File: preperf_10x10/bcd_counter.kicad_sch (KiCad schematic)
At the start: 9 parts, among them U8 4511, U9 D168K

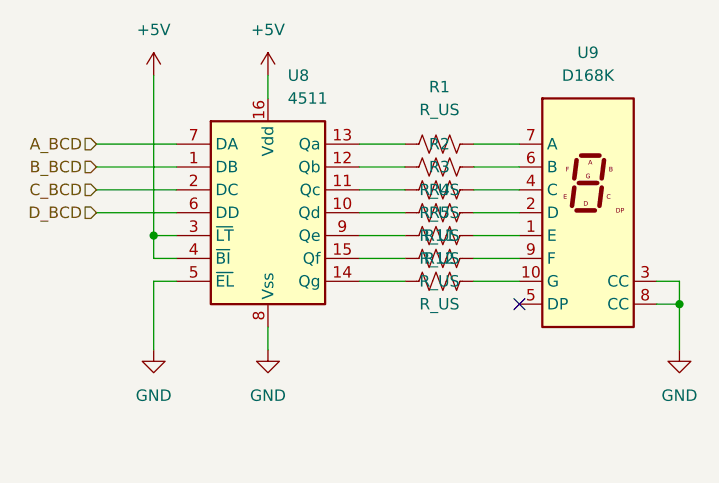
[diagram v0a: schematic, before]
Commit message: "TP2" and "TP3" digital techniques
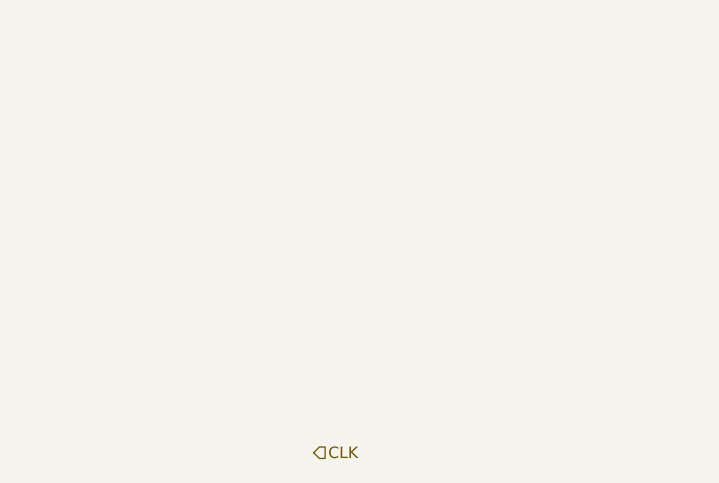
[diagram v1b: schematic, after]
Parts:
- removed R1, R11, R12, R2, R3, R4, R5: R_US, Resistor_THT:R_Axial_DIN0207_L6.3mm_D2.5mm_P2.54mm_Vertical, symbol Device:R_US
- removed U8: 4511, Package_DIP:DIP-16_W7.62mm_Socket, symbol 4xxx_IEEE:4511
- removed U9: D168K, Display_7Segment:D1X8K, symbol Display_Character:D168K
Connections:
- no-connect marks 1 -> 0

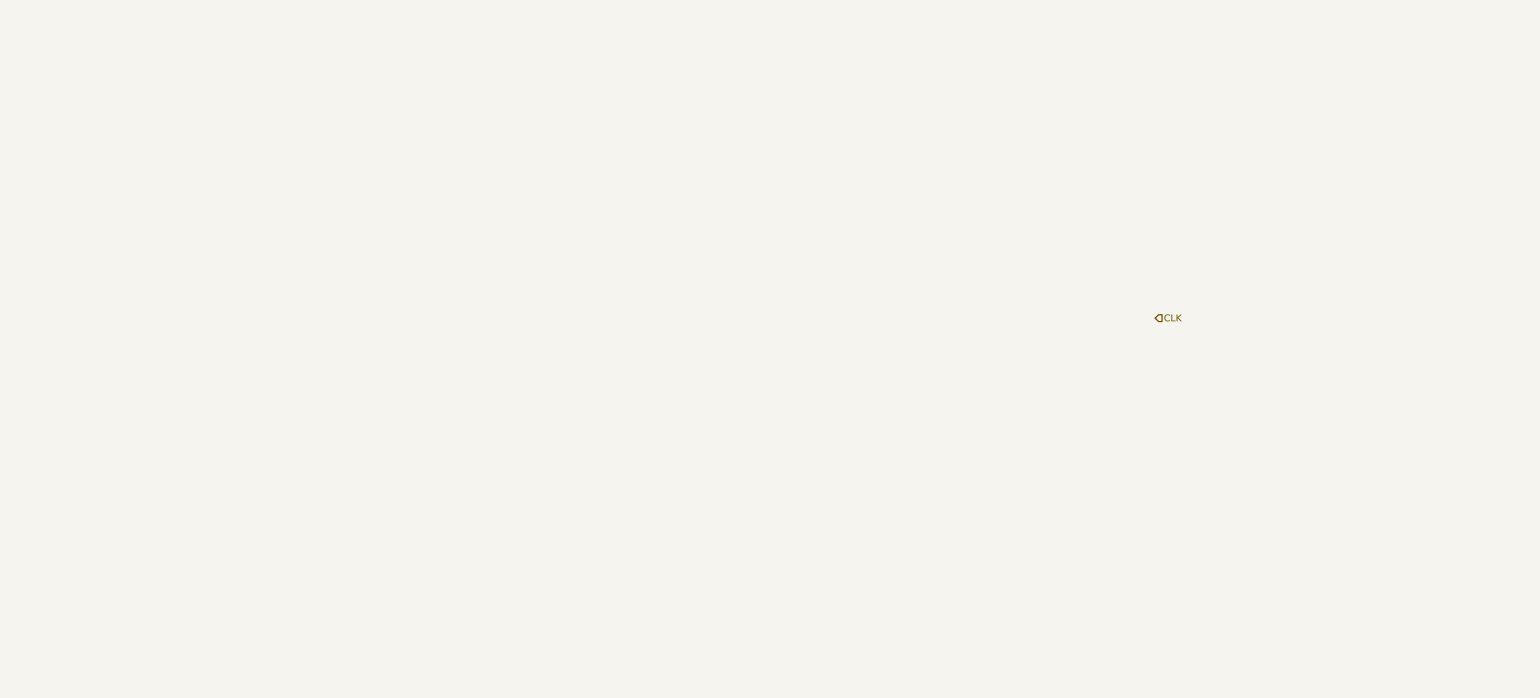
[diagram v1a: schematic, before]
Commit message: Added BCD Up counter with JK FF
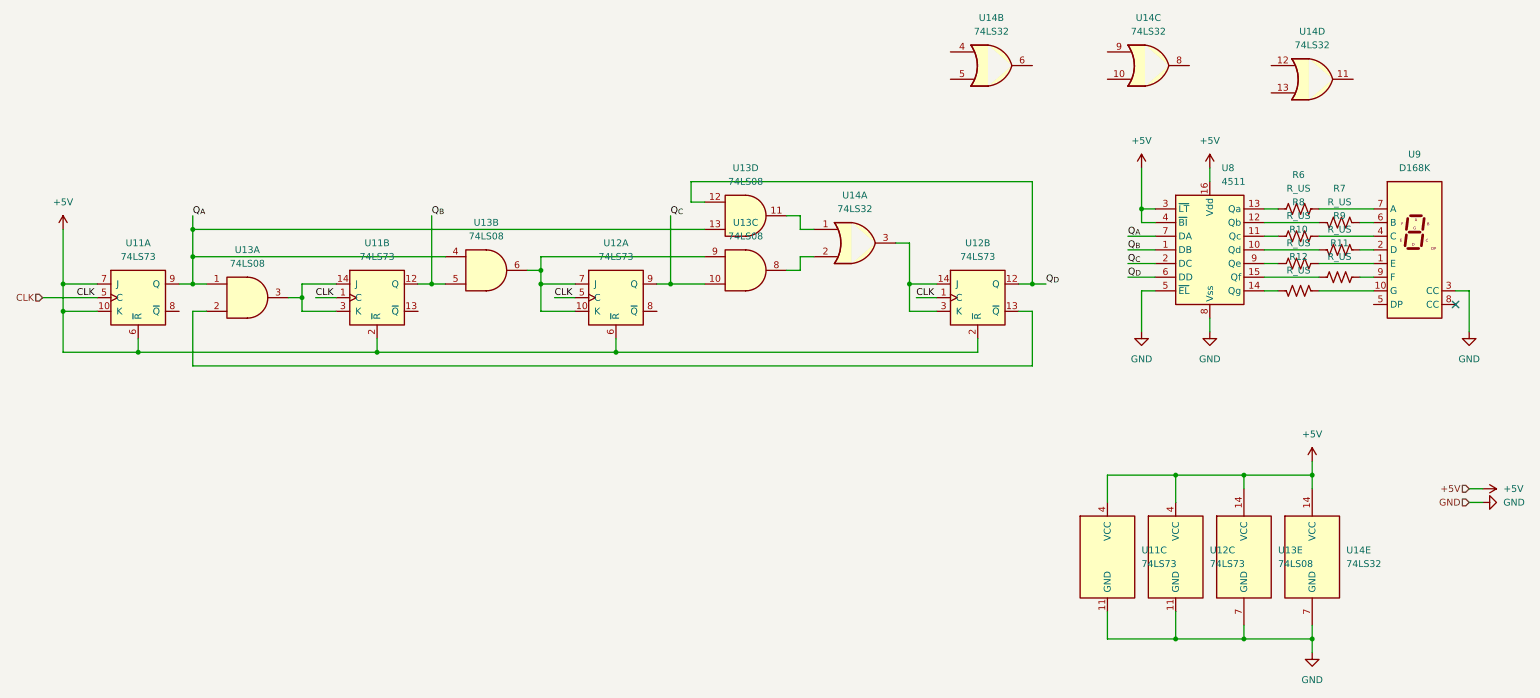
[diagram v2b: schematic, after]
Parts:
- added R10, R11, R12, R6, R7, R8, R9: R_US, Resistor_THT:R_Axial_DIN0207_L6.3mm_D2.5mm_P2.54mm_Vertical, symbol Device:R_US
- added U11, U12: 74LS73, Package_DIP:DIP-14_W7.62mm_Socket, symbol 74xx:74LS73
- added U13: 74LS08, Package_DIP:DIP-14_W7.62mm_Socket, symbol 74xx:74LS08
- added U14: 74LS32, Package_DIP:DIP-14_W7.62mm_Socket, symbol 74xx:74LS32
- added U8: 4511, Package_DIP:DIP-16_W7.62mm_Socket, symbol 4xxx_IEEE:4511
- added U9: D168K, Display_7Segment:D1X8K, symbol Display_Character:D168K
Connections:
- net CLK: now also U11.1 (C), U11.5 (C), U12.1 (C), U12.5 (C)
- new net: U12.13 (~{Q}), U13.2
- new net: U11.14 (J), U11.3 (K), U13.3
- new net: U13.8, U14.2
- new net: U12.10 (K), U12.7 (J), U13.6, U13.9
- new net: R8.1, U8.11 (Qc)
- new net: R8.2, U9.4 (C)
- new net: R9.2, U8.10 (Qd)
- new net: R7.2, U8.12 (Qb)
- new net: R6.1, U8.13 (Qa)
- new net: R12.2, U8.14 (Qg)
- new net: R11.1, U8.15 (Qf)
- new net: R10.1, U8.9 (Qe)
- new net: U13.11, U14.1
- new net: U12.14 (J), U12.3 (K), U14.3
- new net: R6.2, U9.7 (A)
- new net: R12.1, U9.10 (G)
- new net: R10.2, U9.1 (E)
- new net: R7.1, U9.6 (B)
- new net: R11.2, U9.9 (F)
- new net: R9.1, U9.2 (D)
- new net +5V: U11.10 (K), U11.2 (~{R}), U11.4 (VCC), U11.6 (~{R}), U11.7 (J), U12.2 (~{R}), U12.4 (VCC), U12.6 (~{R}), U13.14 (VCC), U14.14 (VCC), U8.16 (Vdd), U8.3 (~{LT}), U8.4 (~{BI})
- new net GND: U11.11 (GND), U12.11 (GND), U13.7 (GND), U14.7 (GND), U8.5 (~{EL}), U8.8 (Vss), U9.3 (CC)
- new net Q_{A}: U11.9 (Q), U13.1, U13.13, U13.4, U8.7 (DA)
- new net Q_{B}: U11.12 (Q), U13.5, U8.1 (DB)
- new net Q_{C}: U12.9 (Q), U13.10, U8.2 (DC)
- new net Q_{D}: U12.12 (Q), U13.12, U8.6 (DD)
- no-connect marks 0 -> 1
